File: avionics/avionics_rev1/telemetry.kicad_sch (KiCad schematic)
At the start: 11 parts, among them U11 MAX-M10S-00B

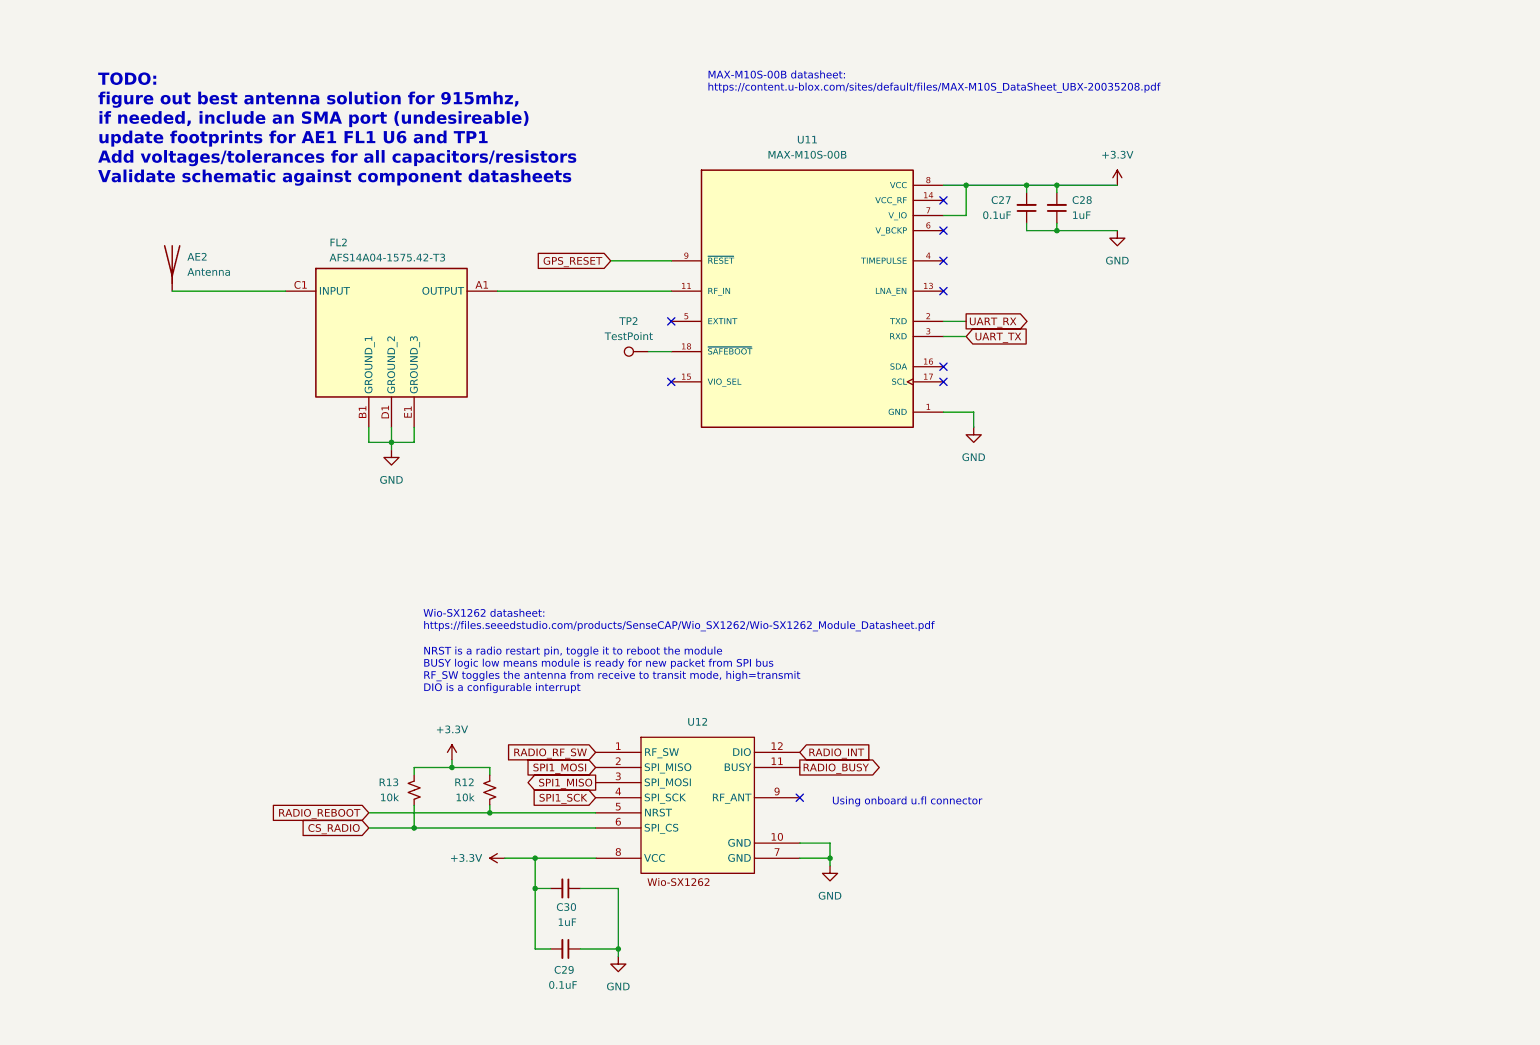
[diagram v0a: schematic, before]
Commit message: cleaned up schematics after codex work
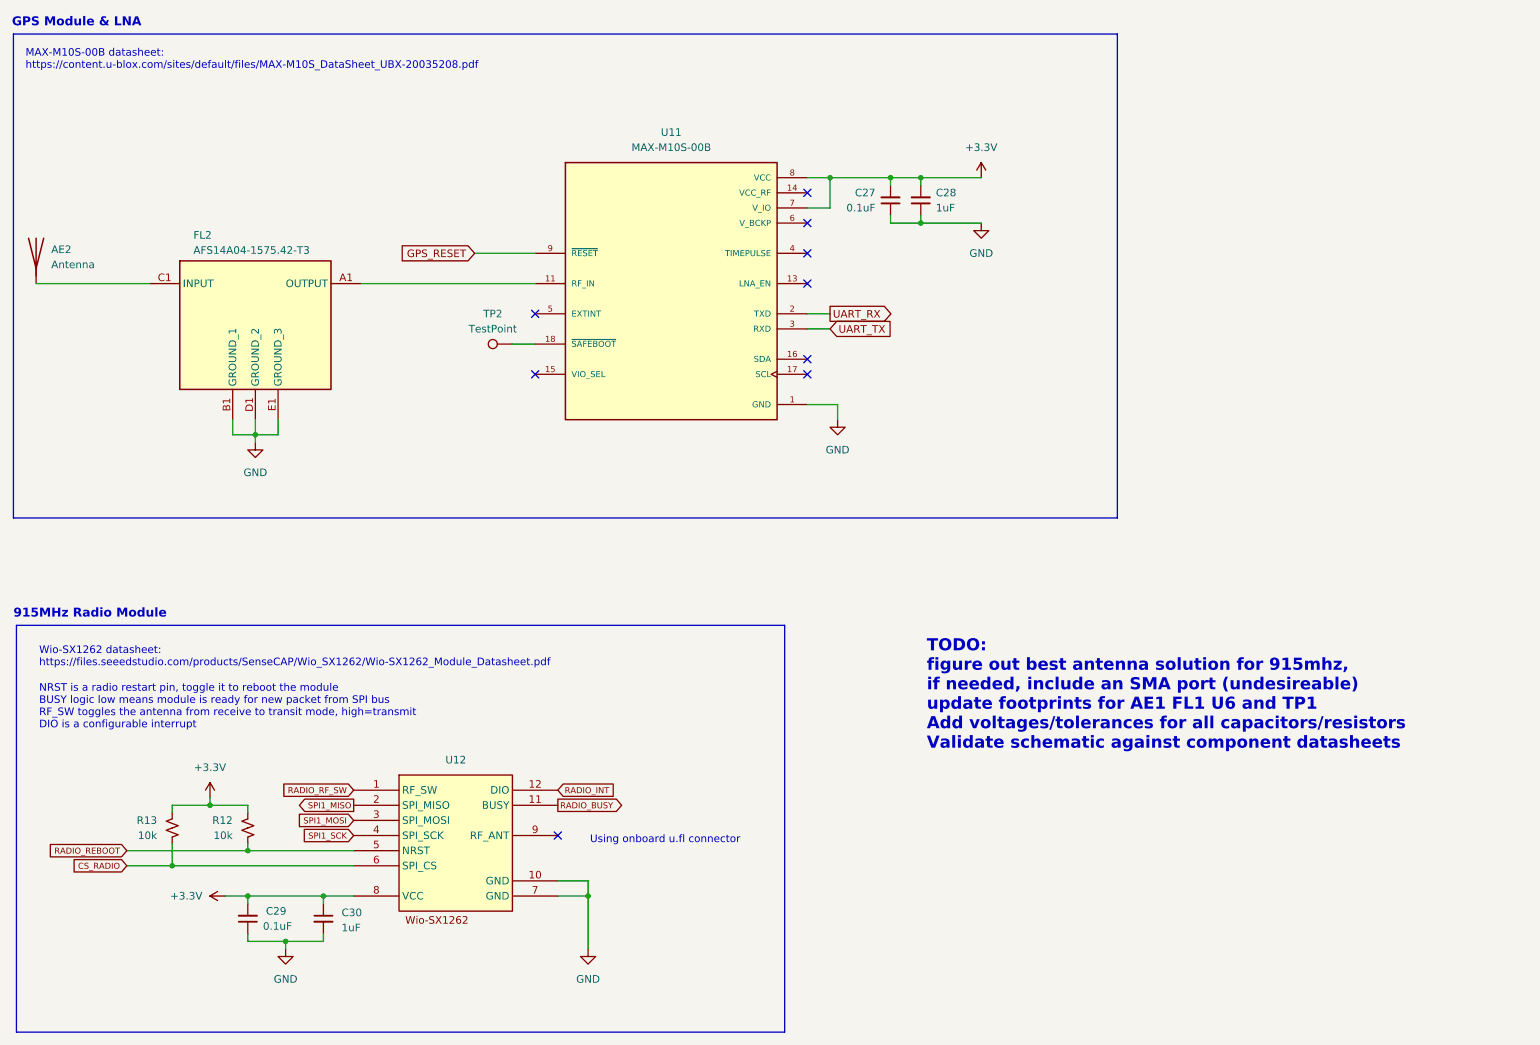
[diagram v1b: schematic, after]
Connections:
- net +3.3V: now also C30.1; no longer C30.2
- net GND: now also C30.2; no longer C30.1
- net SPI1_MISO: now also U12.2 (SPI_MISO); no longer U12.3 (SPI_MOSI)
- net SPI1_MOSI: now also U12.3 (SPI_MOSI); no longer U12.2 (SPI_MISO)
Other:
- note added: "915MHz Radio Module"
- note added: "GPS Module & LNA"
- moved on the sheet: AE2, C27, C28, C29, FL2, R12, R13, TP2, U11, U12

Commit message: fixed ERC errors
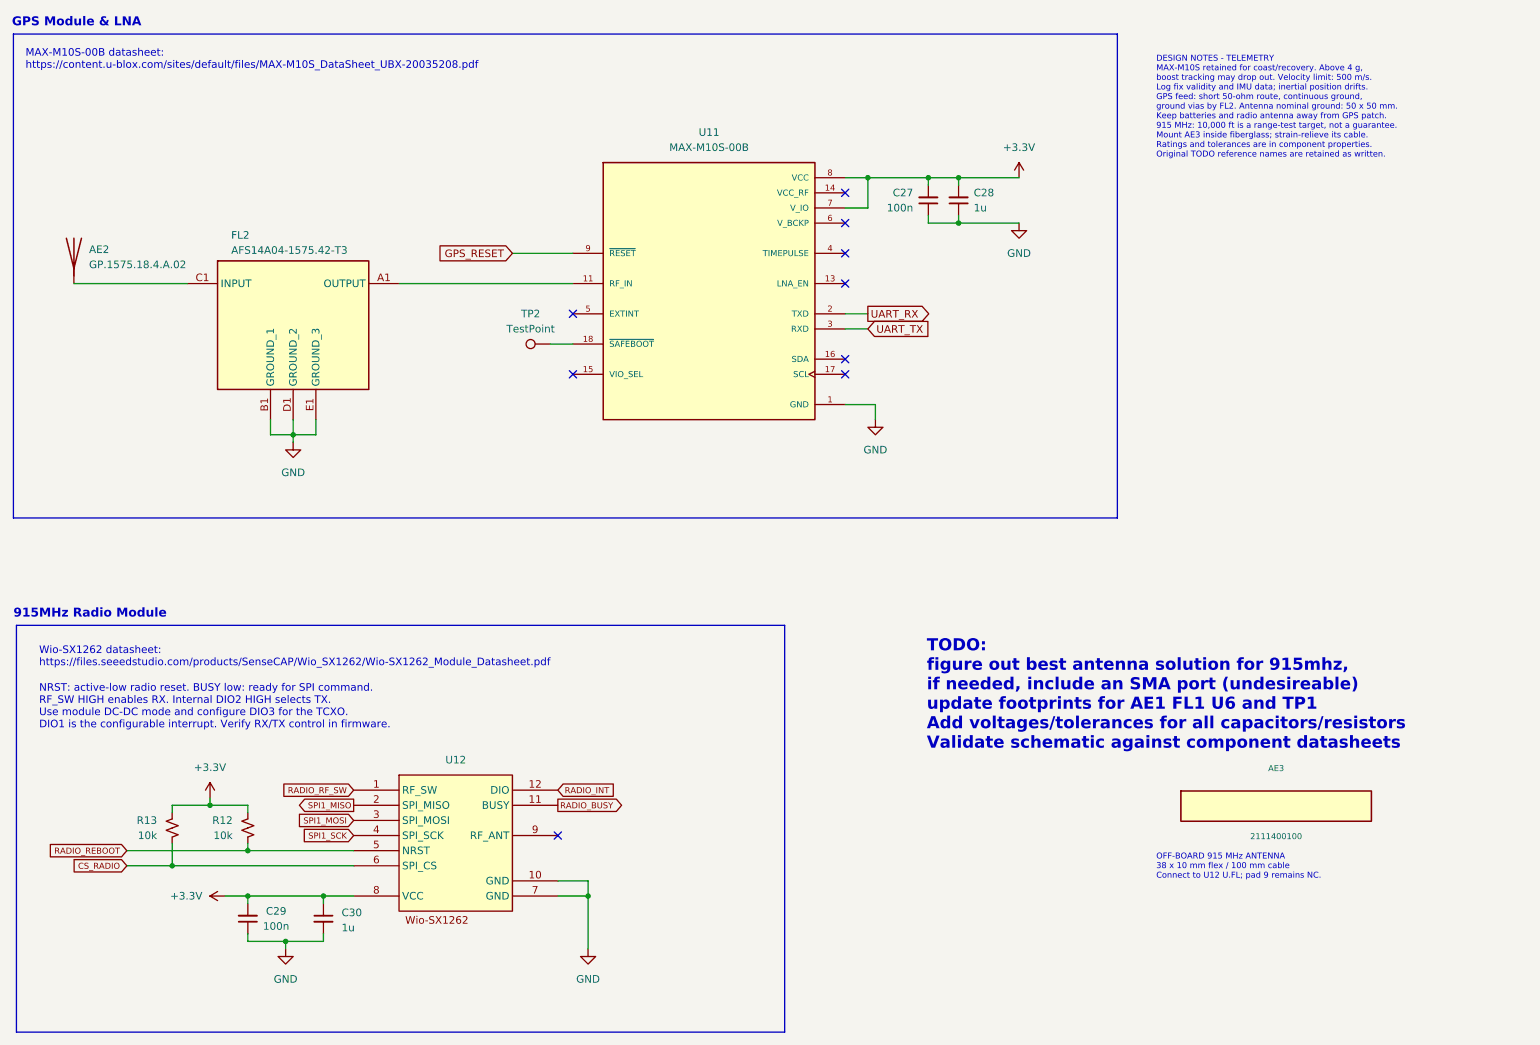
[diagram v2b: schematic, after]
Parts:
- added AE3: 2111400100, symbol rocketry_library:Molex_2111400100_Offboard
- AE2: value Antenna -> GP.1575.18.4.A.02; DigiKey (none) -> https://www.digikey.com/en/products/detail/taoglas-limited/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; MPN (none) -> GP.1575.18.4.A.02; Manufacturer (none) -> Taoglas
- C27, C29: value 0.1uF -> 100n; footprint Capacitor_SMD:C_0201_0603Metric -> Capacitor_SMD:C_0402_1005Metric; symbol Device:C_Small -> rocketry_library:GRM155R71A104KA01D; Dielectric (none) -> X7R; DigiKey (none) -> https://www.digikey.com/en/products/detail/murata-electroni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; MPN (none) -> GRM155R71A104KA01D; Tolerance (none) -> 10%; Voltage (none) -> 10V
- C28, C30: value 1uF -> 1u; footprint Capacitor_SMD:C_0201_0603Metric -> Capacitor_SMD:C_0603_1608Metric; symbol Device:C_Small -> rocketry_library:C1608X7R1A105K080AC; Dielectric (none) -> X7R; DigiKey (none) -> https://www.digikey.com/en/products/detail/tdk/C1608X7R1A10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; MPN (none) -> C1608X7R1A105K080AC; Tolerance (none) -> 10%; Voltage (none) -> 10V
- FL2: footprint AFS14A04157542T3 -> avionics_footprints:AFS14A04157542T3; DigiKey (none) -> https://www.digikey.com/en/products/detail/abracon-llc/AFS1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; MPN (none) -> AFS14A04-1575.42-T3; Manufacturer (none) -> Abracon
- R12, R13: footprint Resistor_SMD:R_0201_0603Metric -> Resistor_SMD:R_0402_1005Metric; symbol Device:R_Small_US -> rocketry_library:RC0402FR-0710KL; DigiKey (none) -> https://www.digikey.com/en/products/detail/yageo/RC0402FR-0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; MPN (none) -> RC0402FR-0710KL; Tolerance (none) -> 1%; Voltage (none) -> 50V
- TP2: footprint (none) -> TestPoint:TestPoint_Pad_D1.0mm; now left out of the parts list
- U11: footprint MAX-M10S-00B:XCVR_MAX-M10S-00B -> avionics_footprints:XCVR_MAX-M10S-00B; DigiKey (none) -> https://www.digikey.com/en/products/detail/u-blox/MAX-M10S-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; MPN (none) -> MAX-M10S-00B; Manufacturer (none) -> u-blox
- U12: value (none) -> Wio-SX1262; DigiKey (none) -> https://www.digikey.com/en/products/detail/seeed-technology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; MPN (none) -> 114993390; Manufacturer (none) -> Seeed Studio
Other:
- note added: "DESIGN NOTES - TELEMETRY MAX-M10S retained for coast/recovery. Above 4 g, boost tracking may drop out. Velocity limit: 500 m/s. Log fix validity and IMU data; inertial position drifts. GPS feed: short 50-ohm route, continuous ground, ground vias by FL2. Antenna nominal ground: 50 x 50 mm. Keep batteries and radio antenna away from GPS patch. 915 MHz: 10,000 ft is a range-test target, not a guaran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"
- note added: "NRST: active-low radio reset. BUSY low: ready for SPI command. RF_SW HIGH enables RX. Internal DIO2 HIGH selects TX. Use module DC-DC mode and configure DIO3 for the TCXO. DIO1 is the configurable interrupt. Verify RX/TX control in firmware."
- note added: "OFF-BOARD 915 MHz ANTENNA 38 x 10 mm flex / 100 mm cable Connect to U12 U.FL; pad 9 remains NC."
- note removed: "NRST is a radio restart pin, toggle it to reboot the module BUSY logic low means module is ready for new packet from SPI bus RF_SW toggles the antenna from receive to transit mode, high=transmit DIO is a configurable interrupt"
- note removed: "Using onboard u.fl connector"
- moved on the sheet: AE2, C27, C28, FL2, TP2, U11
